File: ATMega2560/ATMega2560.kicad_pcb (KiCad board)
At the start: 2 copper layers, 46 parts, among them J1 1x3, J13 1x4, J14 1x4, J15 1x4, J16 1x8, J17 1x2, J18 1x2, J19 1x8, J2 1x3, J20 1x5, J21 1x4, J24 1x2, J25 1x3, J26 1x3, J27 1x3, J28 1x3, J3 1x3, J4 1x3, J5 1x3, J6 1x3, J7 1x3, J8 1x3, K1 G5Q-1, K2 G5Q-1, K3 G5Q-1, K4 G5Q-1

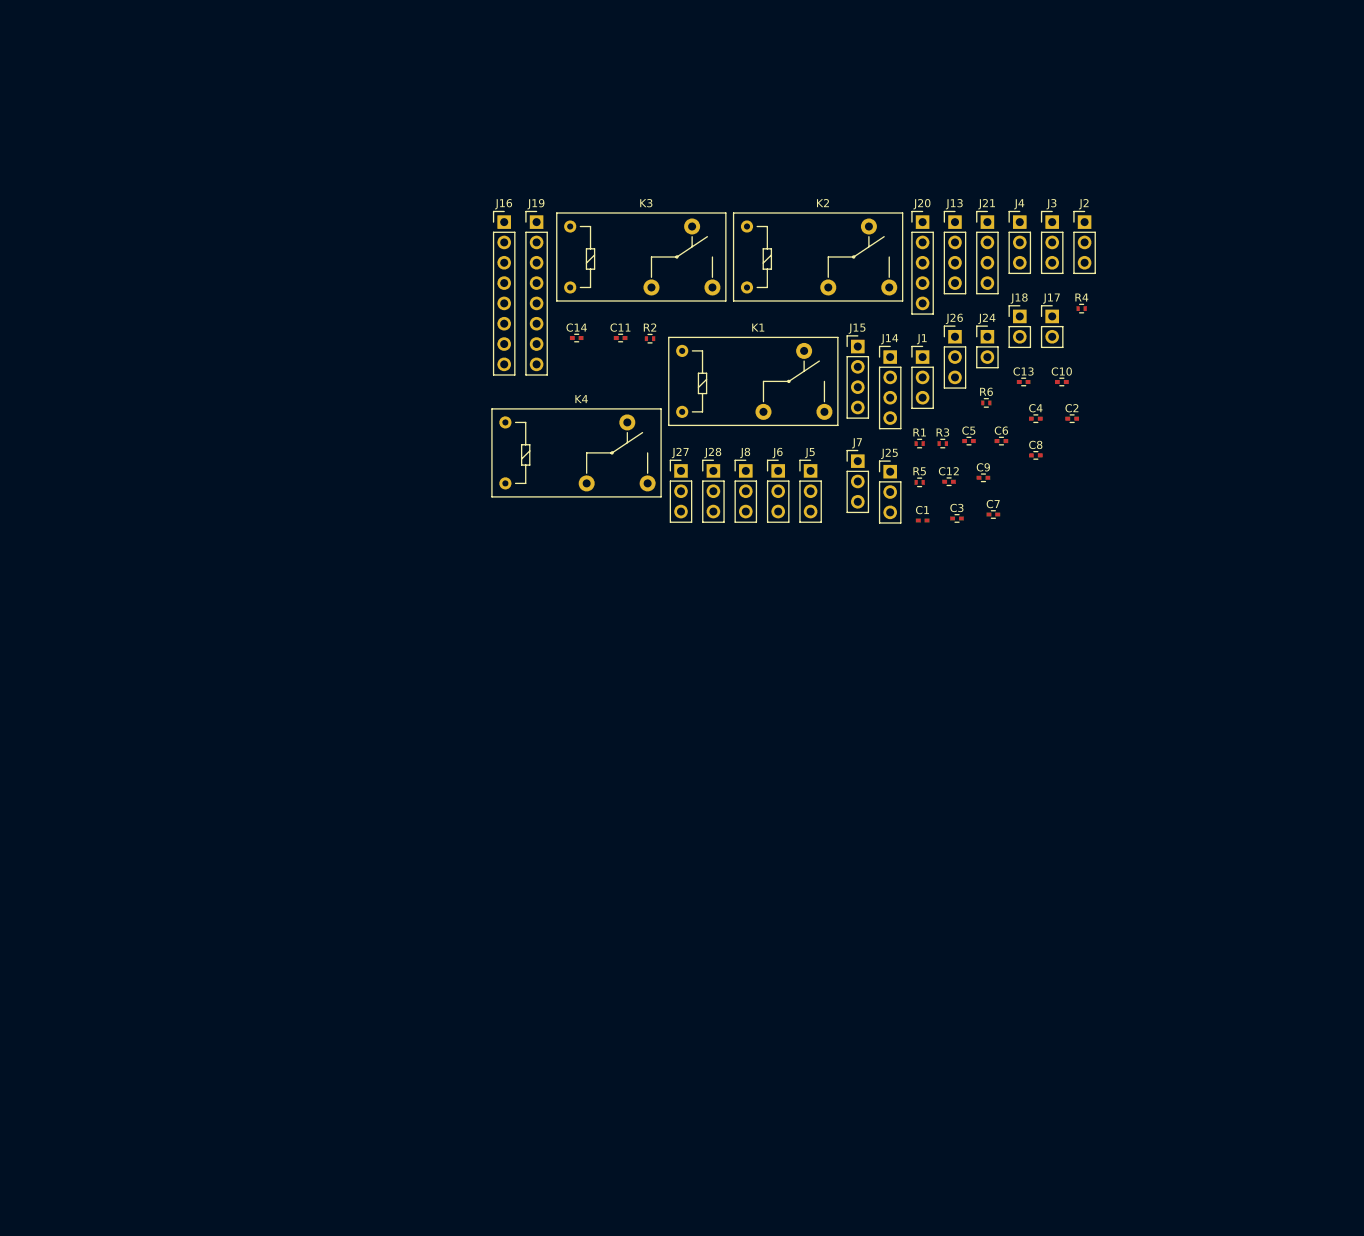
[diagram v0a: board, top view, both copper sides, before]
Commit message: BNC, Relay and Regulator connections are made
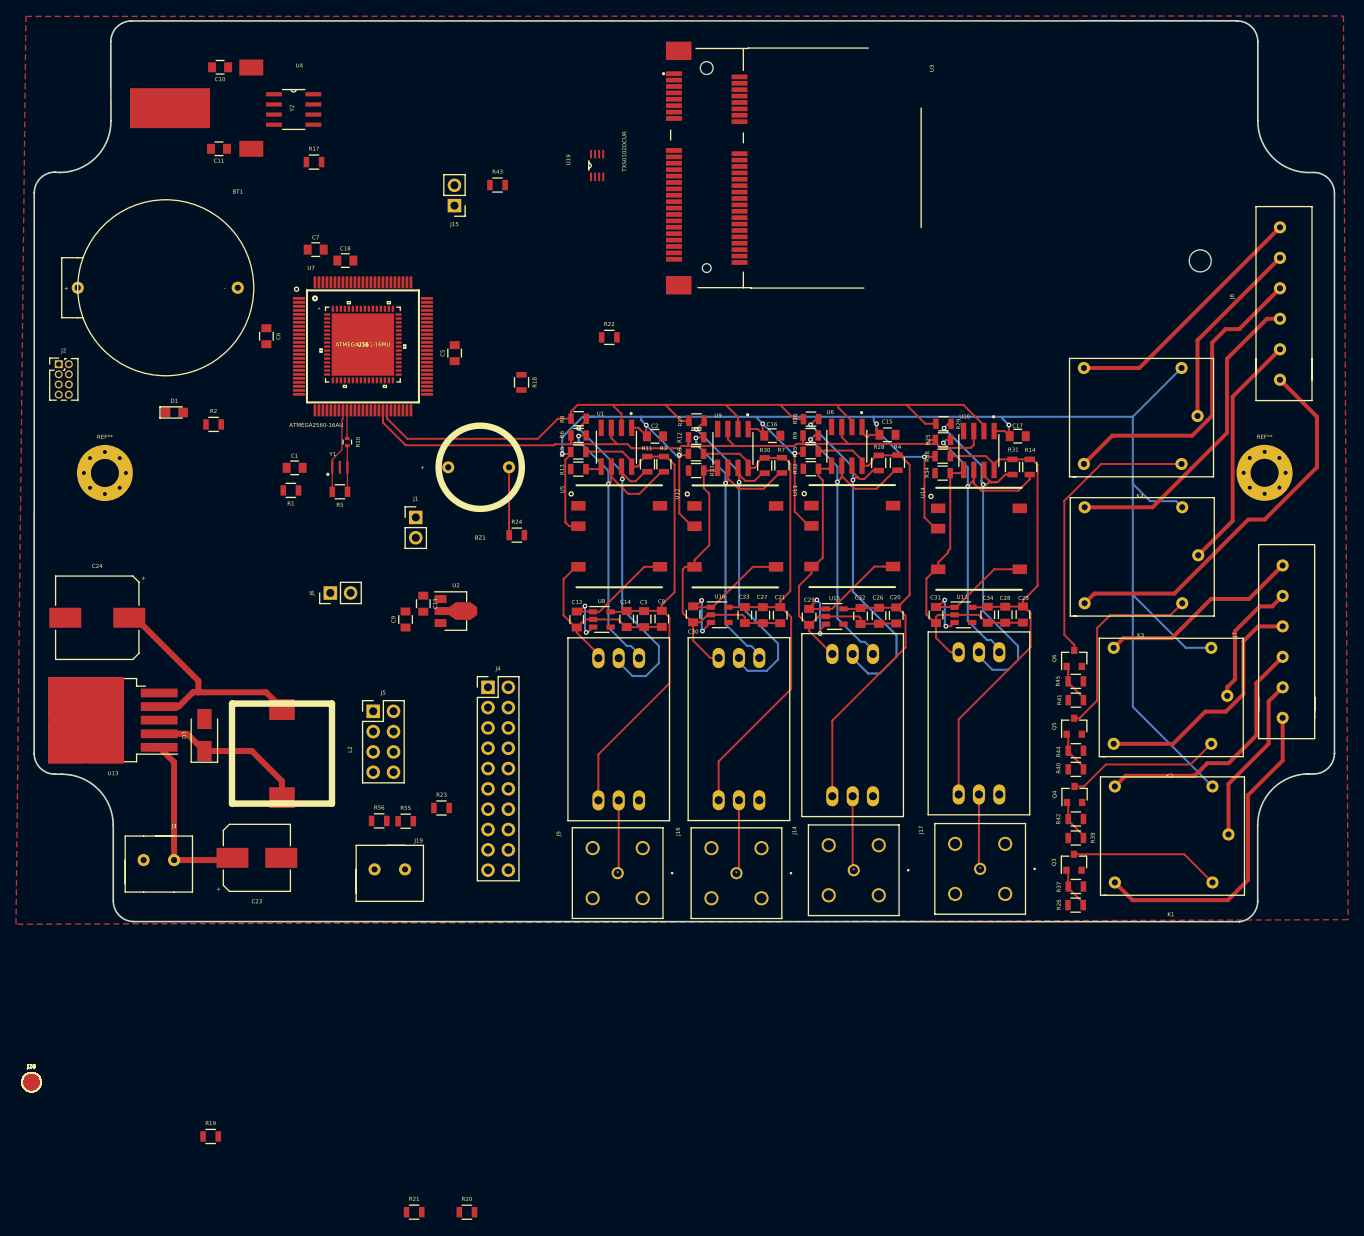
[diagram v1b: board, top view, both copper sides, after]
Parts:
- removed C4: 0.1uF, Capacitors_SMD:C_0402
- removed J26, J27, J28: 1x3, Pin_Headers:Pin_Header_Straight_1x03_Pitch2.54mm
- added ?: , RPi_Hat:RPi_Hat_Mounting_Hole, F.Cu at (223.2, 79.8)
- added BT1: Battery_Cell, footprints:DS1092-04-B6P, F.Cu at (102.8, 83.2)
- added BZ1: Buzzer, footprints:MCW12075, F.Cu at (133.2, 105.6)
- added C15: 0.1uF, Capacitors_SMD:C_0805, F.Cu at (184.1, 101.5)
- added C16: 0.1uF, Capacitors_SMD:C_0805, F.Cu at (169.7, 101.7)
- added C17: 0.1uF, Capacitors_SMD:C_0805, F.Cu at (200.3, 101.7)
- added C18: 0.1uF, Capacitors_SMD:C_0805, F.Cu at (116.3, 79.8)
- added C20: 0.1uF, Capacitors_SMD:C_0805, F.Cu at (185.2, 124.1)
- added C21: 0.1uF, Capacitors_SMD:C_0805, F.Cu at (170.7, 124.1)
- added C23: 100uF, Capacitors_SMD:CP_Elec_8x10, F.Cu at (105.2, 154.4)
- added C24: 1000uF, Capacitors_SMD:CP_Elec_10x10.5, F.Cu at (85.3, 124.4)
- added C25: 0.1uF, Capacitors_SMD:C_0805, F.Cu at (201.0, 124.0)
- added C26: 1uF, Capacitors_SMD:C_0805, F.Cu at (183.0, 124.2)
- added C27: 1uF, Capacitors_SMD:C_0805, F.Cu at (168.5, 124.1)
- added C28: 1uF, Capacitors_SMD:C_0805, F.Cu at (198.8, 124.0)
- added C29: 1uF, Capacitors_SMD:C_0805, F.Cu at (174.3, 124.3)
- added C30: 1uF, Capacitors_SMD:C_0805, F.Cu at (159.8, 124.0)
- added C31: 1uF, Capacitors_SMD:C_0805, F.Cu at (190.1, 124.1)
- added C32: 2.2uF, Capacitors_SMD:C_0805, F.Cu at (180.7, 124.2)
- added C33: 2.2uF, Capacitors_SMD:C_0805, F.Cu at (166.2, 124.1)
- added C34: 2.2uF, Capacitors_SMD:C_0805, F.Cu at (196.6, 124.0)
- added D1: ON, LEDs:LED_0805, F.Cu at (94.9, 98.8)
- added D3: 3A-60V, Diodes_SMD:D_SMA, F.Cu at (98.7, 139.1)
- added EZ1: EZO-hub, footprints:Atlas_Stamp, F.Cu at (150.5, 138.4)
- added EZ2: EZO-hub, footprints:Atlas_Stamp, F.Cu at (179.7, 137.8)
- added EZ3: EZO-hub, footprints:Atlas_Stamp, F.Cu at (165.5, 138.3)
- added EZ4: EZO-hub, footprints:Atlas_Stamp, F.Cu at (195.5, 137.6)
- added J10: TEST_VBat, TestPoint:TestPoint_Pad_D2.0mm, F.Cu at (77.1, 182.5)
- added J11: TEST_Reset, TestPoint:TestPoint_Pad_D2.0mm, F.Cu at (77.1, 182.5)
- added J12: TEST_MISO, TestPoint:TestPoint_Pad_D2.0mm, F.Cu at (77.1, 182.5)
- added J22: TEST_GND, TestPoint:TestPoint_Pad_D2.0mm, F.Cu at (77.1, 182.5)
- added J23: TEST_RX0, TestPoint:TestPoint_Pad_D2.0mm, F.Cu at (77.1, 182.5)
- added J9: BNC_1, footprints:5-1634503-1, F.Cu at (150.3, 156.3)
- added L2: 100uH, footprints:L_SMD_12.5x12.5, F.Cu at (108.4, 140.9)
- added Q3: NMOS, TO_SOT_Packages_SMD:SOT-23, F.Cu at (207.4, 155.0)
- added Q4: NMOS, TO_SOT_Packages_SMD:SOT-23, F.Cu at (207.4, 146.5)
- added Q5: NMOS, TO_SOT_Packages_SMD:SOT-23, F.Cu at (207.4, 138.0)
- added Q6: NMOS, TO_SOT_Packages_SMD:SOT-23, F.Cu at (207.4, 129.5)
- added R10: 27R, Resistors_SMD:R_0402, F.Cu at (116.5, 102.5)
- added R11: 4.7K, Resistors_SMD:R_0805, F.Cu at (154.1, 105.2)
- added R12: DNP, Resistors_SMD:R_0805, F.Cu at (160.1, 101.9)
- added R13: DNP, Resistors_SMD:R_0805, F.Cu at (145.4, 105.8)
- added R14: 4.7K, Resistors_SMD:R_0805, F.Cu at (201.8, 105.6)
- added R15: DNP, Resistors_SMD:R_0805, F.Cu at (145.4, 103.7)
- added R16: DNP, Resistors_SMD:R_0805, F.Cu at (174.5, 99.6)
- added R17: 10K, Resistors_SMD:R_0805, F.Cu at (112.4, 67.5)
- added R18: 4.7K, Resistors_SMD:R_0805, F.Cu at (138.3, 95.0)
- added R19: 100R, Resistors_SMD:R_0805, F.Cu at (99.5, 189.3)
- added R20: 100R, Resistors_SMD:R_0805, F.Cu at (131.5, 198.7)
- added R21: 100R, Resistors_SMD:R_0805, F.Cu at (124.9, 198.7)
- added R22: 4.7K, Resistors_SMD:R_0805, F.Cu at (149.3, 89.4)
- added R23: 4.7K, Resistors_SMD:R_0805, F.Cu at (128.3, 148.2)
- added R24: 100R, Resistors_SMD:R_0805, F.Cu at (137.7, 114.1)
- added R25: DNP, Resistors_SMD:R_0805, F.Cu at (191.0, 102.2)
- added R26: 1K, Resistors_SMD:R_0805, F.Cu at (207.6, 160.3)
- added R27: DNP, Resistors_SMD:R_0805, F.Cu at (160.2, 99.8)
- added R28: 4.7K, Resistors_SMD:R_0805, F.Cu at (183.0, 105.1)
- added R29: DNP, Resistors_SMD:R_0805, F.Cu at (191.1, 100.2)
- added R30: 4.7K, Resistors_SMD:R_0805, F.Cu at (168.7, 105.4)
- added R31: 4.7K, Resistors_SMD:R_0805, F.Cu at (199.7, 105.6)
- added R32: DNP, Resistors_SMD:R_0805, F.Cu at (174.5, 105.8)
- added R33: DNP, Resistors_SMD:R_0805, F.Cu at (160.1, 106.0)
- added R34: DNP, Resistors_SMD:R_0805, F.Cu at (190.9, 106.3)
- added R35: DNP, Resistors_SMD:R_0805, F.Cu at (174.4, 103.7)
- added R36: DNP, Resistors_SMD:R_0805, F.Cu at (160.1, 103.9)
- added R37: 10K, Resistors_SMD:R_0805, F.Cu at (207.6, 158.0)
- added R38: DNP, Resistors_SMD:R_0805, F.Cu at (190.9, 104.2)
- added R39: 1K, Resistors_SMD:R_0805, F.Cu at (207.6, 151.9)
- added R40: 1K, Resistors_SMD:R_0805, F.Cu at (207.6, 143.4)
- added R41: 1K, Resistors_SMD:R_0805, F.Cu at (207.6, 134.7)
- added R42: 10K, Resistors_SMD:R_0805, F.Cu at (207.6, 149.6)
- added R43: 10K, Resistors_SMD:R_0805, F.Cu at (135.3, 70.3)
- added R44: 10K, Resistors_SMD:R_0805, F.Cu at (207.6, 141.0)
- added R45: 10K, Resistors_SMD:R_0805, F.Cu at (207.6, 132.4)
- added R55: 1M, Resistors_SMD:R_0805, F.Cu at (123.8, 149.8)
- added R56: 100K, Resistors_SMD:R_0805, F.Cu at (120.5, 149.8)
- added R7: 4.7K, Resistors_SMD:R_0805, F.Cu at (170.9, 105.4)
- added R8: DNP, Resistors_SMD:R_0805, F.Cu at (145.4, 99.5)
- added R9: DNP, Resistors_SMD:R_0805, F.Cu at (174.4, 101.6)
- added REF**: MountingHole_3.5mm_Pad_Via, Mounting_Holes:MountingHole_3.5mm_Pad_Via, F.Cu at (231.2, 106.3)
- added REF**: MountingHole_3.5mm_Pad_Via, Mounting_Holes:MountingHole_3.5mm_Pad_Via, F.Cu at (86.2, 106.3)
- added U1: SI8600, SOIC127P600X175-8N:SOIC127P600X175-8N, F.Cu at (150.2, 103.1)
- added U10: SI8600, SOIC127P600X175-8N:SOIC127P600X175-8N, F.Cu at (195.5, 103.5)
- added U11: R1SE-0505, R1SE-0505-R:SOIC254P1110X700-5N, F.Cu at (179.7, 114.2)
- added U12: R1SE-0505, R1SE-0505-R:SOIC254P1110X700-5N, F.Cu at (165.0, 114.2)
- added U13: LM2576, TO_SOT_Packages_SMD:TO-263-5_TabPin3, F.Cu at (87.2, 137.2)
- added U14: R1SE-0505, R1SE-0505-R:SOIC254P1110X700-5N, F.Cu at (195.5, 114.5)
- added U15: LD2981ABM, TO_SOT_Packages_SMD:SOT-23-5, F.Cu at (177.4, 124.3)
- added U16: LD2981ABM, TO_SOT_Packages_SMD:SOT-23-5, F.Cu at (163.1, 124.0)
- added U17: LD2981ABM, TO_SOT_Packages_SMD:SOT-23-5, F.Cu at (193.5, 124.1)
- added U18: ATMEGA2561-16MU, footprints:ATMEGA2561V-8MU, F.Cu at (118.5, 90.3)
- added U19: TXS0102DCUR, TXS0102DCUR:SOP50P310X90-8N, F.Cu at (147.8, 67.9)
- added U2: L78L33ABUTR, TO_SOT_Packages_SMD:SOT-89-3, F.Cu at (129.7, 123.6)
- added U3: MPCIE-Socket, 2041119-1:TE_2041119-1, F.Cu at (161.5, 68.2)
- added U4: DS1302, DS1302ZN_:SOIC127P600X175-8N, F.Cu at (109.8, 60.9)
- added U5: R1SE-0505, R1SE-0505-R:SOIC254P1110X700-5N, F.Cu at (150.5, 114.2)
- added U6: SI8600, SOIC127P600X175-8N:SOIC127P600X175-8N, F.Cu at (179.0, 103.0)
- added U7: ATMEGA2560-16AU, ATMEGA2560-16AU:QFP50P1600X1600X120-100N, F.Cu at (118.5, 90.5)
- added U8: LD2981ABM, TO_SOT_Packages_SMD:SOT-23-5, F.Cu at (148.3, 124.6)
- added U9: SI8600, SOIC127P600X175-8N:SOIC127P600X175-8N, F.Cu at (164.7, 103.3)
- added Y1: 16Mhz, CSTCE16M0V53-R0:OSC_CSTCE16M0V53-R0, F.Cu at (115.6, 105.6)
- added Y2: 32.768 KHz, footprints:R38-32.768, F.Cu at (104.5, 60.7)
- C1: footprint Capacitors_SMD:C_0402_NoSilk -> Capacitors_SMD:C_0805
- C10: value 0.1uF -> 22pF; footprint Capacitors_SMD:C_0402 -> Capacitors_SMD:C_0805
- C11: value 220uF -> 22pF; footprint Capacitors_SMD:C_0402 -> Capacitors_SMD:C_0805
- C12: value 22uF -> 1uF; footprint Capacitors_SMD:C_0402 -> Capacitors_SMD:C_0805
- C13: value 100uF -> 0.1uF; footprint Capacitors_SMD:C_0402 -> Capacitors_SMD:C_0805
- C14: value 1000uF -> 2.2uF; footprint Capacitors_SMD:C_0402 -> Capacitors_SMD:C_0805
- C2, C7, C8: footprint Capacitors_SMD:C_0402 -> Capacitors_SMD:C_0805
- C3: value 0.1uF -> 1uF; footprint Capacitors_SMD:C_0402 -> Capacitors_SMD:C_0805
- C5, C6: value 22pF -> 0.1uF; footprint Capacitors_SMD:C_0402 -> Capacitors_SMD:C_0805
- C9: value 0.1uF -> 0.33uF; footprint Capacitors_SMD:C_0402 -> Capacitors_SMD:C_0805
- J1: value 1x3 -> RX/TX; footprint Pin_Headers:Pin_Header_Straight_1x03_Pitch2.54mm -> Pin_Headers:Pin_Header_Straight_1x02_Pitch2.54mm
- J13: value 1x4 -> TEST_5V; footprint Pin_Headers:Pin_Header_Straight_1x04_Pitch2.54mm -> TestPoint:TestPoint_Pad_D2.0mm
- J14: value 1x4 -> BNC_1; footprint Pin_Headers:Pin_Header_Straight_1x04_Pitch2.54mm -> footprints:5-1634503-1
- J15: value 1x4 -> BTN; footprint Pin_Headers:Pin_Header_Straight_1x04_Pitch2.54mm -> Pin_Headers:Pin_Header_Straight_1x02_Pitch2.54mm
- J16: value 1x8 -> BNC_1; footprint Pin_Headers:Pin_Header_Straight_1x08_Pitch2.54mm -> footprints:5-1634503-1
- J17: value 1x2 -> BNC_1; footprint Pin_Headers:Pin_Header_Straight_1x02_Pitch2.54mm -> footprints:5-1634503-1
- J18: value 1x2 -> TEST_MOSI; footprint Pin_Headers:Pin_Header_Straight_1x02_Pitch2.54mm -> TestPoint:TestPoint_Pad_D2.0mm
- J19: value 1x8 -> Analog_IN_01x02; footprint Pin_Headers:Pin_Header_Straight_1x08_Pitch2.54mm -> footprints:15EDGVC-3.81-02P-14-00AH
- J2: value 1x3 -> Prog_02x04_Odd_Even; footprint Pin_Headers:Pin_Header_Straight_1x03_Pitch2.54mm -> Pin_Headers:Pin_Header_Straight_2x04_Pitch1.27mm
- J20: value 1x5 -> TEST_3.3V; footprint Pin_Headers:Pin_Header_Straight_1x05_Pitch2.54mm -> TestPoint:TestPoint_Pad_D2.0mm
- J21: value 1x4 -> TEST_SCK; footprint Pin_Headers:Pin_Header_Straight_1x04_Pitch2.54mm -> TestPoint:TestPoint_Pad_D2.0mm
- J24: value 1x2 -> TEST_TX0; footprint Pin_Headers:Pin_Header_Straight_1x02_Pitch2.54mm -> TestPoint:TestPoint_Pad_D2.0mm
- J25: value 1x3 -> TEST_VDD_EXT; footprint Pin_Headers:Pin_Header_Straight_1x03_Pitch2.54mm -> TestPoint:TestPoint_Pad_D2.0mm
- J3: value 1x3 -> Power_IN_01x02; footprint Pin_Headers:Pin_Header_Straight_1x03_Pitch2.54mm -> footprints:15EDGVC-3.81-02P-14-00AH
- J4: value 1x3 -> Sensors_02x10_Odd_Even; footprint Pin_Headers:Pin_Header_Straight_1x03_Pitch2.54mm -> Pin_Headers:Pin_Header_Straight_2x10_Pitch2.54mm
- J5: value 1x3 -> IO_02x04_Odd_Even; footprint Pin_Headers:Pin_Header_Straight_1x03_Pitch2.54mm -> Pin_Headers:Pin_Header_Straight_2x04_Pitch2.54mm
- J6: value 1x3 -> I2C; footprint Pin_Headers:Pin_Header_Straight_1x03_Pitch2.54mm -> Pin_Headers:Pin_Header_Straight_1x02_Pitch2.54mm
- J7, J8: value 1x3 -> Screw_Terminal_01x06; footprint Pin_Headers:Pin_Header_Straight_1x03_Pitch2.54mm -> footprints:15EGTVC-3.81-06P-14-00AH
- K1, K2, K3, K4: footprint Relays_THT:Relay_SPDT_OMRON-G5Q -> footprints:HJR-3FF-S-Z-4
- R1, R2: footprint Resistors_SMD:R_0402 -> Resistors_SMD:R_0805
- R3: value 1M -> 4.7K; footprint Resistors_SMD:R_0402 -> Resistors_SMD:R_0805
- R4: value 27R -> 4.7K; footprint Resistors_SMD:R_0402 -> Resistors_SMD:R_0805
- R5: value 10K -> 1M; footprint Resistors_SMD:R_0402 -> Resistors_SMD:R_0805
- R6: value 4.7K -> DNP; footprint Resistors_SMD:R_0402 -> Resistors_SMD:R_0805
- moved J21 160.7 mm to (77.1, 182.5)
- moved J13 157.7 mm to (77.1, 182.5)
- moved J18 156.3 mm to (77.1, 182.5)
- moved J20 154.8 mm to (77.1, 182.5)
- moved J24 151.5 mm to (77.1, 182.5)
- moved J3 138.8 mm to (91.1, 154.7), turned to 180 degrees
- moved J25 131.7 mm to (77.1, 182.5)
- moved J2 129.5 mm to (80.5, 92.7)
- moved C10 112.3 mm to (100.6, 55.6), turned to 180 degrees
- moved C6 92.8 mm to (106.4, 89.2), turned to 270 degrees
- moved C7 91.0 mm to (112.6, 78.4)
- moved J4 88.3 mm to (134.1, 133.1)
- moved J16 86.4 mm to (165.2, 156.3)
- moved J19 83.4 mm to (119.9, 155.9), turned to 180 degrees
- moved K1 80.8 mm to (219.5, 151.5)
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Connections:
- C11 pad 1: +3.3V -> Net-(C11-Pad1)
- C12 pad 1: +5V -> /GND_ISO1
- C12 pad 2: GND -> Net-(C12-Pad2)
- C13 pad 1: VBat -> +3.3V
- C14 pad 1: +5V -> /VDD_ISO1
- C14 pad 2: GND -> /GND_ISO1
- C2 pad 1: +5V -> GND
- C2 pad 2: GND -> +5V
- C3 pad 1: +5V -> /GND_ISO1
- C3 pad 2: GND -> /VDD_ISO1
- C5 pad 1: Net-(C5-Pad1) -> +5V
- C6 pad 1: Net-(C6-Pad1) -> +5V
- C7 pad 1: Net-(C7-Pad1) -> +5V
- C7 pad 2: /RESET -> GND
- C8 pad 1: +5V -> /GND_ISO1
- C8 pad 2: GND -> /VDD_ISO1
- C9 pad 1: GND -> +5V
- C9 pad 2: +3.3V -> GND
- J1 pad 1: SCL -> /TX1
- J1 pad 2: SDA -> /RX1
- J13 pad 1: GND -> +5V
- J14 pad 1: +5V -> Net-(EZ2-Pad5)
- J14 pad 2: /TR2 -> Net-(EZ2-Pad6)
- J15 pad 2: /TR1 -> /D28
- J16 pad 1: /D22 -> Net-(EZ3-Pad5)
- J16 pad 2: /D23 -> Net-(EZ3-Pad6)
- J17 pad 1: SCL -> Net-(EZ4-Pad5)
- J17 pad 2: SDA -> Net-(EZ4-Pad6)
- J18 pad 1: /RX1 -> /ARD_MOSI
- J19 pad 1: /A0 -> Net-(J19-Pad1)
- J19 pad 2: /A1 -> GND
- J2 pad 1: SCL -> /ARD_SCK
- J2 pad 2: SDA -> /RX0
- J2 pad 3: GND -> /ARD_MOSI
- J20 pad 1: Net-(C7-Pad1) -> +3.3V
- J21 pad 1: +3.3V -> /ARD_SCK
- J24 pad 1: GND -> /TX0
- J25 pad 1: Net-(J25-Pad1) -> /VDD_EXT
- J3 pad 1: SCL -> VBat
- J3 pad 2: SDA -> GND
- J4 pad 1: SCL -> GND
- J4 pad 2: SDA -> GND
- J5 pad 1: +5V -> /D25
- J5 pad 2: Net-(J5-Pad2) -> /A3
- J5 pad 3: Net-(J5-Pad3) -> /D26
- J6 pad 1: +5V -> SCL
- J6 pad 2: Net-(J10-Pad1) -> SDA
- J7 pad 1: +5V -> Net-(J7-Pad1)
- J7 pad 2: Net-(J11-Pad1) -> Net-(J7-Pad2)
- J7 pad 3: Net-(J11-Pad2) -> Net-(J7-Pad3)
- J8 pad 1: +5V -> Net-(J8-Pad1)
- J8 pad 2: Net-(J12-Pad1) -> Net-(J8-Pad2)
- J8 pad 3: Net-(J12-Pad2) -> Net-(J8-Pad3)
- K1 pad 1: /R1 -> Net-(K1-Pad1)
- K1 pad 2: Net-(J26-Pad2) -> Net-(J7-Pad5)
- K1 pad 3: Net-(J26-Pad3) -> Net-(J7-Pad6)
- K1 pad 4: Net-(J26-Pad1) -> Net-(J7-Pad4)
- K2 pad 1: /R2 -> Net-(K2-Pad1)
- K2 pad 2: Net-(J27-Pad2) -> Net-(J7-Pad2)
- K2 pad 3: Net-(J27-Pad3) -> Net-(J7-Pad3)
- K2 pad 4: Net-(J27-Pad1) -> Net-(J7-Pad1)
- K3 pad 1: /R3 -> Net-(K3-Pad1)
- K3 pad 2: Net-(J25-Pad2) -> Net-(J8-Pad5)
- K3 pad 3: Net-(J25-Pad3) -> Net-(J8-Pad6)
- K3 pad 4: Net-(J25-Pad1) -> Net-(J8-Pad4)
- K4 pad 1: /R4 -> Net-(K4-Pad1)
- K4 pad 2: Net-(J28-Pad2) -> Net-(J8-Pad2)
- K4 pad 3: Net-(J28-Pad3) -> Net-(J8-Pad3)
- K4 pad 4: Net-(J28-Pad1) -> Net-(J8-Pad1)
- R3 pad 1: Net-(R3-Pad1) -> /VDD_ISO1
- R3 pad 2: Net-(R3-Pad2) -> Net-(EZ1-Pad3)
- R4 pad 1: Net-(R4-Pad1) -> /VDD_ISO3
- R4 pad 2: Net-(R3-Pad1) -> Net-(EZ2-Pad3)
- R5 pad 1: /MISO -> Net-(R10-Pad2)
- R5 pad 2: /MOSI -> /XTAL-
- R6 pad 1: +5V -> SCL
- R6 pad 2: /DS18B20 -> Net-(EZ1-Pad3)
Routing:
- net +5V: track 0.00 -> 271.5 mm, vias 0 -> 8
- net SDA: track 0.00 -> 104.0 mm
- net SCL: track 0.00 -> 91.6 mm
- net /VDD_ISO3: track 0.00 -> 67.0 mm
- net /VDD_ISO1: track 0.00 -> 66.6 mm
- net /VDD_ISO2: track 0.00 -> 66.4 mm
- net /VDD_ISO4: track 0.00 -> 65.1 mm
- net Net-(J8-Pad6): track 0.00 -> 48.9 mm
- net Net-(EZ1-Pad2): track 0.00 -> 48.5 mm, vias 0 -> 2
- net Net-(EZ2-Pad2): track 0.00 -> 48.1 mm, vias 0 -> 2
- net Net-(EZ3-Pad2): track 0.00 -> 47.6 mm, vias 0 -> 2
- net Net-(EZ4-Pad2): track 0.00 -> 47.2 mm, vias 0 -> 2
- net Net-(EZ1-Pad3): track 0.00 -> 43.3 mm, vias 0 -> 2
- net Net-(EZ4-Pad3): track 0.00 -> 42.5 mm, vias 0 -> 2
- net Net-(EZ2-Pad3): track 0.00 -> 42.3 mm, vias 0 -> 2
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- added copper zone on F.Cu, net GND
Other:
- board outline added: 162.5 x 112.6 mm
- net class Default: via_drill 0.4 -> 0.3
- rule pad_to_mask_clearance: 0.2 -> 0
- rule trace_min: 0.2 -> 0.01
